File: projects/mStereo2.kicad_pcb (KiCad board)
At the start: 4 copper layers, 159.5 x 120 mm, 125 parts, among them P101 CONN_AMANERO, P102 Screw-term 1x2, P103 Screw-term 1X3, P104 XLR-MALE, P105 XLR-MALE, U101 ISO7640, U102 CDCLVC1104, U103 MCP100-315DI, U104 SRC4192, U201 LT1761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

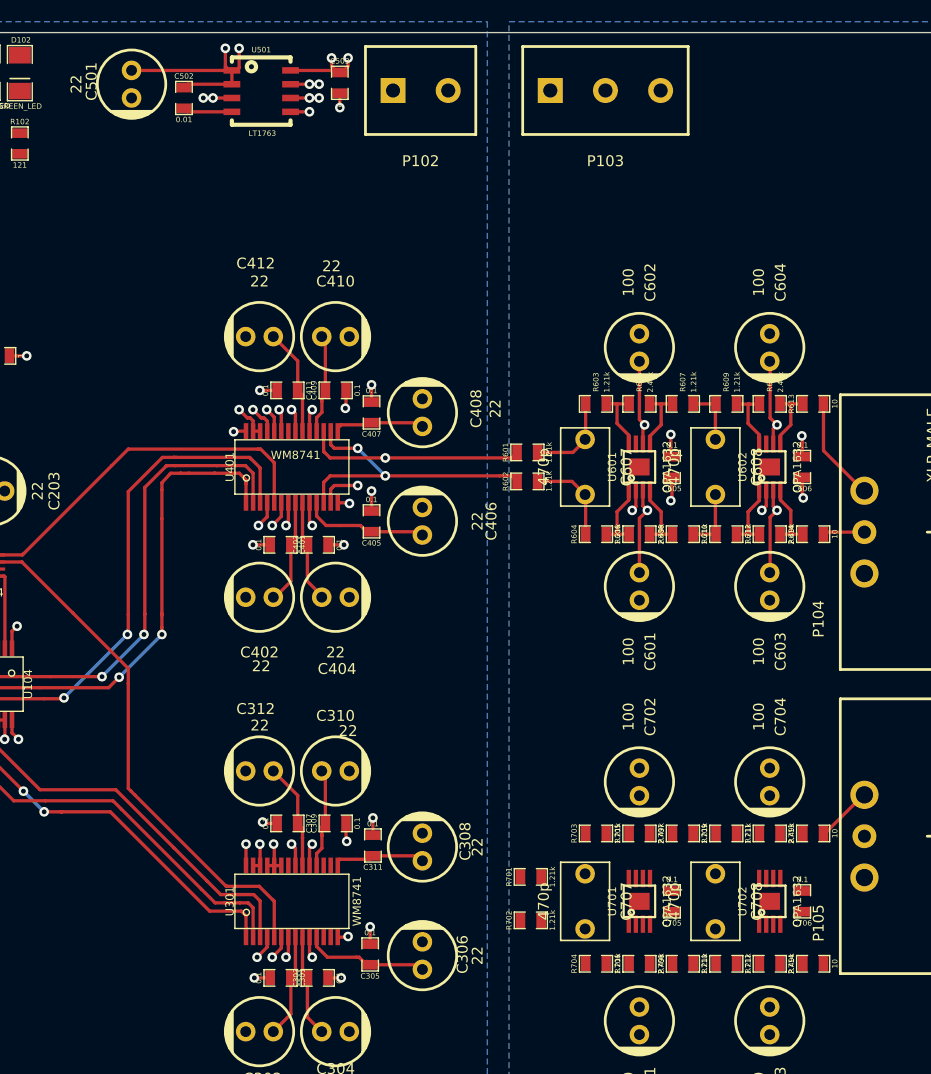
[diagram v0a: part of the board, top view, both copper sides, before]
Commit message: more routing and 3v3 power component placement
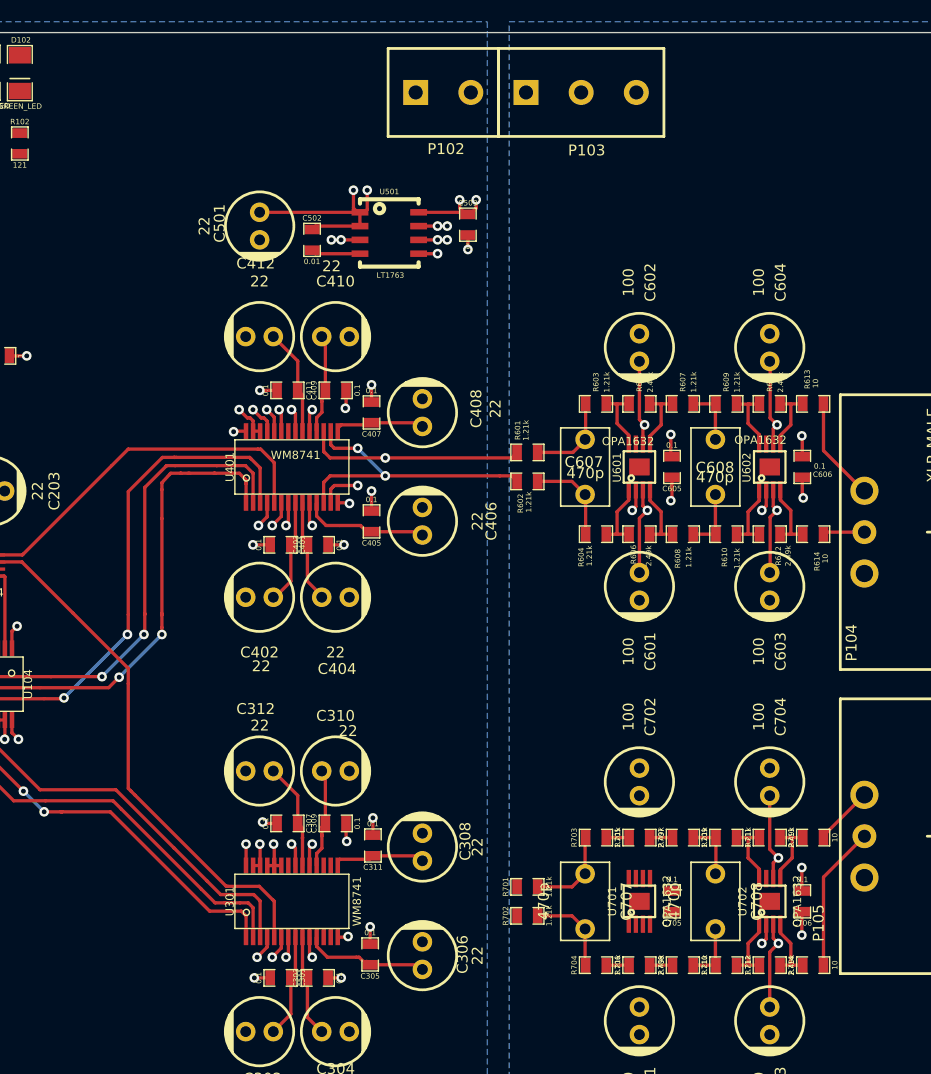
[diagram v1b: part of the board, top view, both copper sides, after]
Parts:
- moved C501 17.6 mm to (122.0, 52.8)
- moved C502 17.6 mm to (126.9, 54.1)
- moved C503 17.6 mm to (141.2, 52.7)
- moved U501 17.6 mm to (134.0, 53.5)
- moved P103 2.24 mm to (151.6, 40.5)
- moved P102 2.09 mm to (138.9, 40.5)
- moved R701 0.97 mm to (146.7, 113.7)
- moved R702 0.52 mm to (146.7, 116.3)
- moved R703 0.38 mm to (153.0, 109.1)
- moved R705 0.38 mm to (157.0, 109.1)
- moved R707 0.38 mm to (161.0, 109.1)
- moved R709 0.38 mm to (165.0, 109.1)
- moved R711 0.38 mm to (169.0, 109.1)
- moved R713 0.38 mm to (173.0, 109.1)
- moved R704 0.13 mm to (153.0, 120.9)
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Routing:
- net /FILTER_R/VOUT-: track 0.00 -> 13.4 mm
- net -12V: track 25.4 -> 38.3 mm, vias 4 -> 6
- net +12V: track 25.7 -> 38.5 mm, vias 4 -> 6
- net Net-(C707-Pad2): track 0.00 -> 8.22 mm
- net Net-(C707-Pad1): track 0.00 -> 8.21 mm
- net Net-(R712-Pad2): track 0.00 -> 6.53 mm
- net Net-(R710-Pad2): track 0.00 -> 6.49 mm
- net Net-(R711-Pad2): track 0.00 -> 6.32 mm
- net Net-(R709-Pad2): track 0.00 -> 6.29 mm
- net Net-(C708-Pad2): track 0.00 -> 5.45 mm
- net Net-(C708-Pad1): track 0.00 -> 5.45 mm
- net Net-(R706-Pad2): track 0.00 -> 2.10 mm
- net Net-(R705-Pad2): track 0.00 -> 2.10 mm
- net Net-(R704-Pad2): track 0.00 -> 2.10 mm
- net Net-(R703-Pad2): track 0.00 -> 2.10 mm
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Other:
- board text added: "Add polarization labels (+ / -) on XLR & power connectors"

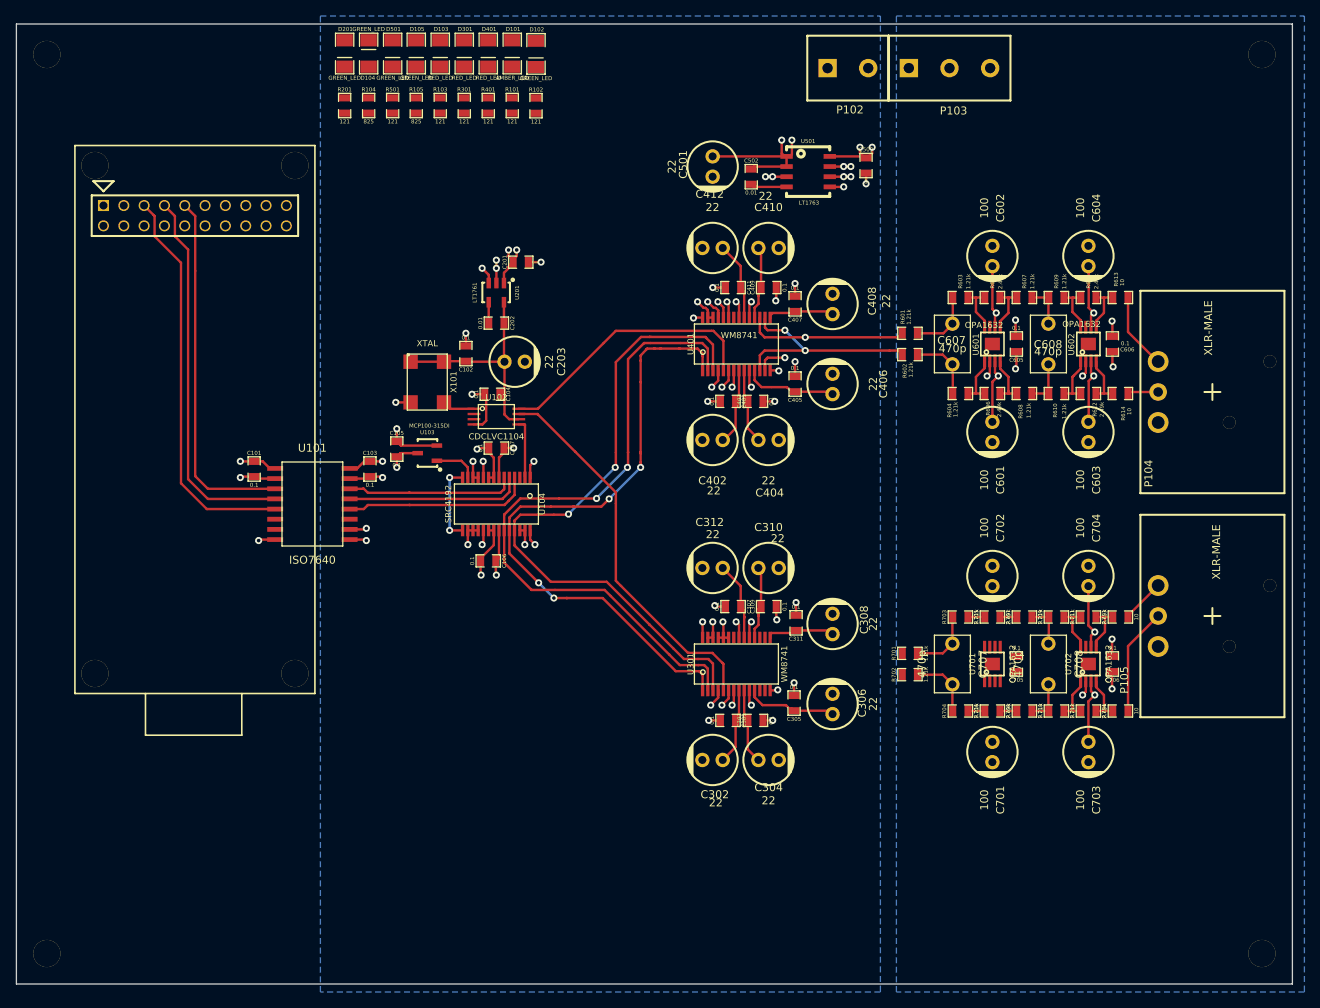
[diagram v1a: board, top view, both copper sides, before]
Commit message: place and route all LEDs; append to future additions list
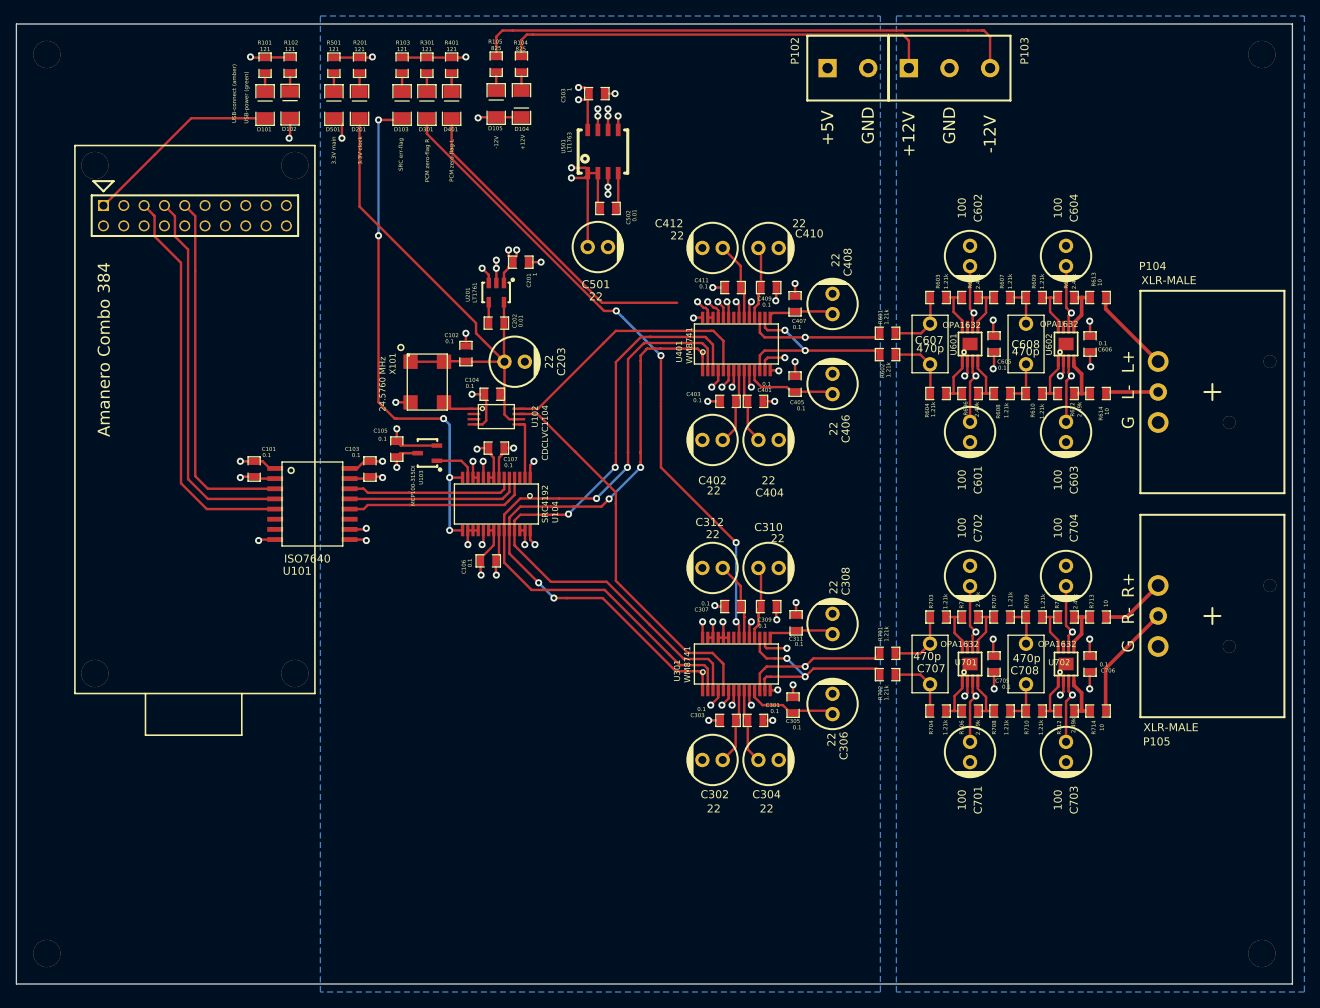
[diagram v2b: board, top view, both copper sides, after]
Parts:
- D101: value AMBER_LED -> USB-connect (amber)
- D102: value GREEN_LED -> USB-power (green)
- D103: value RED_LED -> SRC err-flag
- D104: value GREEN_LED -> +12V
- D105: value GREEN_LED -> -12V
- D201: value GREEN_LED -> 3.3V clock
- D301: value RED_LED -> PCM zero-flag R
- D401: value RED_LED -> PCM zero-flag L
- D501: value GREEN_LED -> 3.3V main
- X101: value XTAL -> 24.5760 MHz
- moved C503 34.8 mm to (107.6, 43.7), turned to 0 degrees
- moved D101 31.6 mm to (66.1, 45.1), turned to 90 degrees
- moved D102 31.4 mm to (69.2, 45.1), turned to 90 degrees
- moved R101 31.3 mm to (66.1, 40.2), turned to 90 degrees
- moved R102 31.2 mm to (69.2, 40.1), turned to 90 degrees
- moved U501 25.8 mm to (108.3, 50.9), turned to 90 degrees
- moved D104 20.1 mm to (98.1, 45.0), turned to 270 degrees
- moved R104 19.8 mm to (98.1, 40.0)
- moved C502 18.3 mm to (109.0, 58.1), turned to 0 degrees
- moved C501 17.5 mm to (107.7, 62.9), turned to 0 degrees
- moved D105 11.8 mm to (95.0, 45.0), turned to 90 degrees
- moved R105 11.2 mm to (95.0, 40.0), turned to 90 degrees
- moved D501 9.77 mm to (74.7, 45.1), turned to 90 degrees
- moved R501 8.91 mm to (74.7, 40.2), turned to 90 degrees
- moved D103 8.01 mm to (83.2, 45.1), turned to 90 degrees
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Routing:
- net -12V: track 38.3 -> 119.9 mm, vias 6 -> 8
- net Net-(D301-Pad1): track 2.12 -> 82.2 mm, vias 1 -> 4
- net +12V: track 38.5 -> 106.0 mm, vias 6 -> 8
- net Net-(D103-Pad1): track 9.85 -> 64.8 mm, vias 2 -> 5
- net Net-(D401-Pad1): track 2.13 -> 42.4 mm
- net VCC: track 28.5 -> 66.4 mm
- net /FILTER_R/VIN-: track 0.00 -> 25.6 mm, vias 0 -> 2
- net /FILTER_R/VIN+: track 0.00 -> 25.4 mm, vias 0 -> 2
- net Net-(D101-Pad1): track 0.00 -> 24.7 mm
- net DGND: track 110.2 -> 130.6 mm, vias 50 -> 54
- net GNDA: track 6.63 -> 11.6 mm, vias 2 -> 3
- net Net-(R706-Pad2): track 2.10 -> 6.49 mm
- net Net-(R705-Pad2): track 2.10 -> 6.29 mm
- net Net-(R704-Pad2): track 2.10 -> 6.27 mm
- net Net-(R703-Pad2): track 2.10 -> 6.26 mm
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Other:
- net class high-i added: clearance 0.2032, trace_width 0.4572, via_dia 0.889, via_drill 0.635
- board text added: "+12V"
- board text added: "+5V"
- board text added: "-12V"
- board text added: "Add board notes (i.e. date, rev, name, etc.)"
- board text added: "Add i2s bus-line trace labels (LRCK, BCK, MCK, DATA)"
- board text added: "Amanero Combo 384"
- board text added: "G"
- board text added: "GND"
- board text added: "L+"
- board text added: "L-"
- board text added: "R+"
- board text added: "R-"
- board text removed: "Add board notes (i.e. voltage labels, date, rev, name, etc.)"
- board text removed: "Make keepout for a USB jack near XLR connectors"

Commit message: add dimensions, begin repositioning silkscreen reference numbers and component values
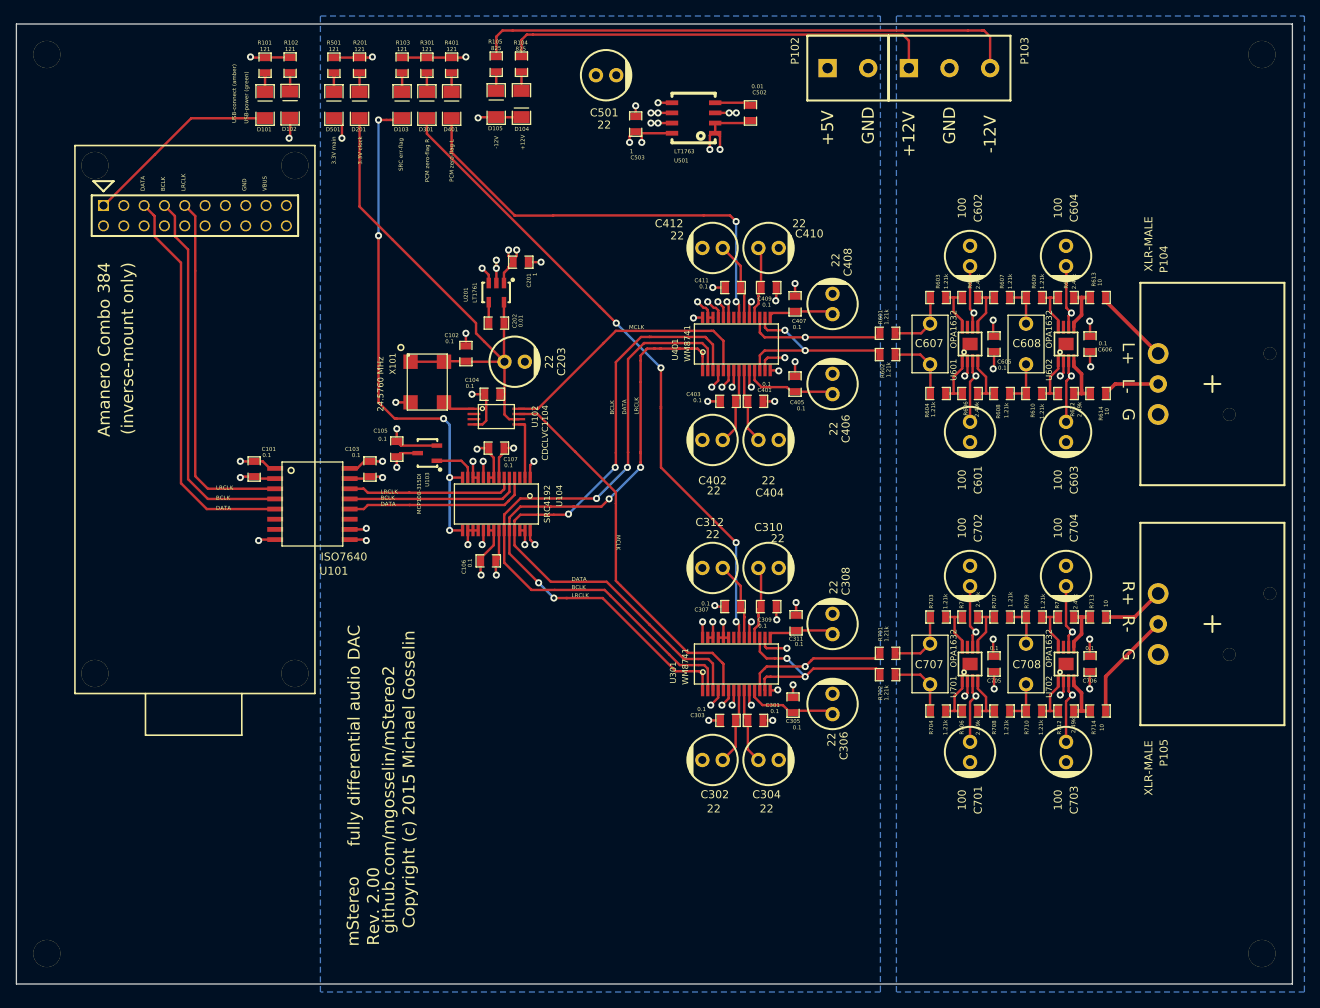
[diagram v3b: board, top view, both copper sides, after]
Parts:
- moved C501 21.5 mm to (108.7, 41.4)
- moved C502 21.4 mm to (126.8, 46.1), turned to 90 degrees
- moved U501 12.1 mm to (119.7, 46.8), turned to 180 degrees
- moved C503 6.17 mm to (112.4, 47.5), turned to 90 degrees
- moved P104 1.00 mm to (184.5, 80.0)
- moved P105 1.00 mm to (184.5, 110.0)
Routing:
- net Net-(D401-Pad1): track 42.4 -> 55.6 mm, vias 1 -> 2
- net VDD: track 88.9 -> 79.7 mm
- net /FILTER_R/VOUT-: track 14.6 -> 13.6 mm
- net /FILTER_L/VOUT+: track 10.7 -> 9.72 mm
- net Net-(D301-Pad1): track 82.2 -> 81.3 mm
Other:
- board text added: "(inverse-mount only)"
- board text added: "+ x-direction"
- board text added: "+ y-direction"
- board text added: "BCLK"
- board text added: "Copyright (c) 2015 Michael Gosselin"
- board text added: "DATA"
- board text added: "LRCLK"
- board text added: "M3 [thru] (4 places)"
- board text added: "MCLK"
- board text added: "Rev. 2.00"
- board text added: "VBUS"
- board text added: "fully differential audio DAC"
- board text added: "github.com/mgosselin/mStereo2"
- board text added: "mStereo"
- board text added: "origin"
- board text removed: "Key part info (ie xtal feq., connector part no's and channel L/R)"
- board text removed: "LEFT"
- board text removed: "RIGHT"

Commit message: rearrage silkscreen
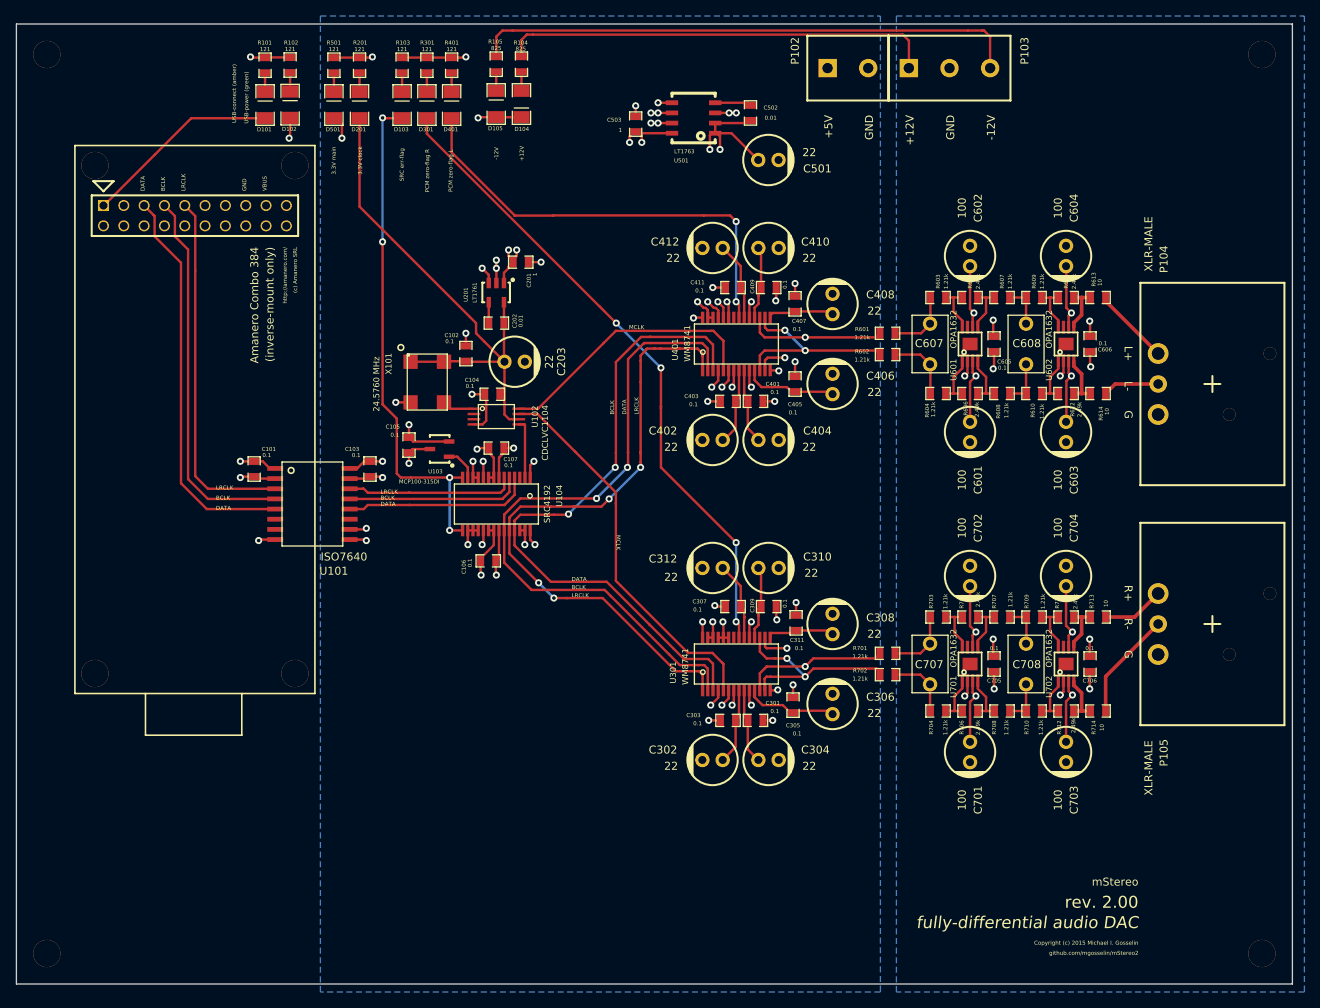
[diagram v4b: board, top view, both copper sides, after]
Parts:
- moved C501 22.9 mm to (129.0, 52.0)
- moved C105 1.61 mm to (84.1, 87.6)
- moved U103 1.61 mm to (87.9, 88.1)
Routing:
- net VDD: track 79.7 -> 86.5 mm
- net /~RST: track 5.49 -> 4.22 mm
- net Net-(D103-Pad1): track 64.8 -> 64.3 mm, vias 5 -> 4
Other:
- board text added: "(c) Amanero SRL"
- board text added: "Copyright (c) 2015 Michael I. Gosselin"
- board text added: "fully-differential audio DAC"
- board text added: "http://amanero.com/"
- board text added: "rev. 2.00"
- board text removed: "Copyright (c) 2015 Michael Gosselin"
- board text removed: "Rev. 2.00"
- board text removed: "fully differential audio DAC"
